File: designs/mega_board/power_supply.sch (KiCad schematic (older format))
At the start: 0 parts

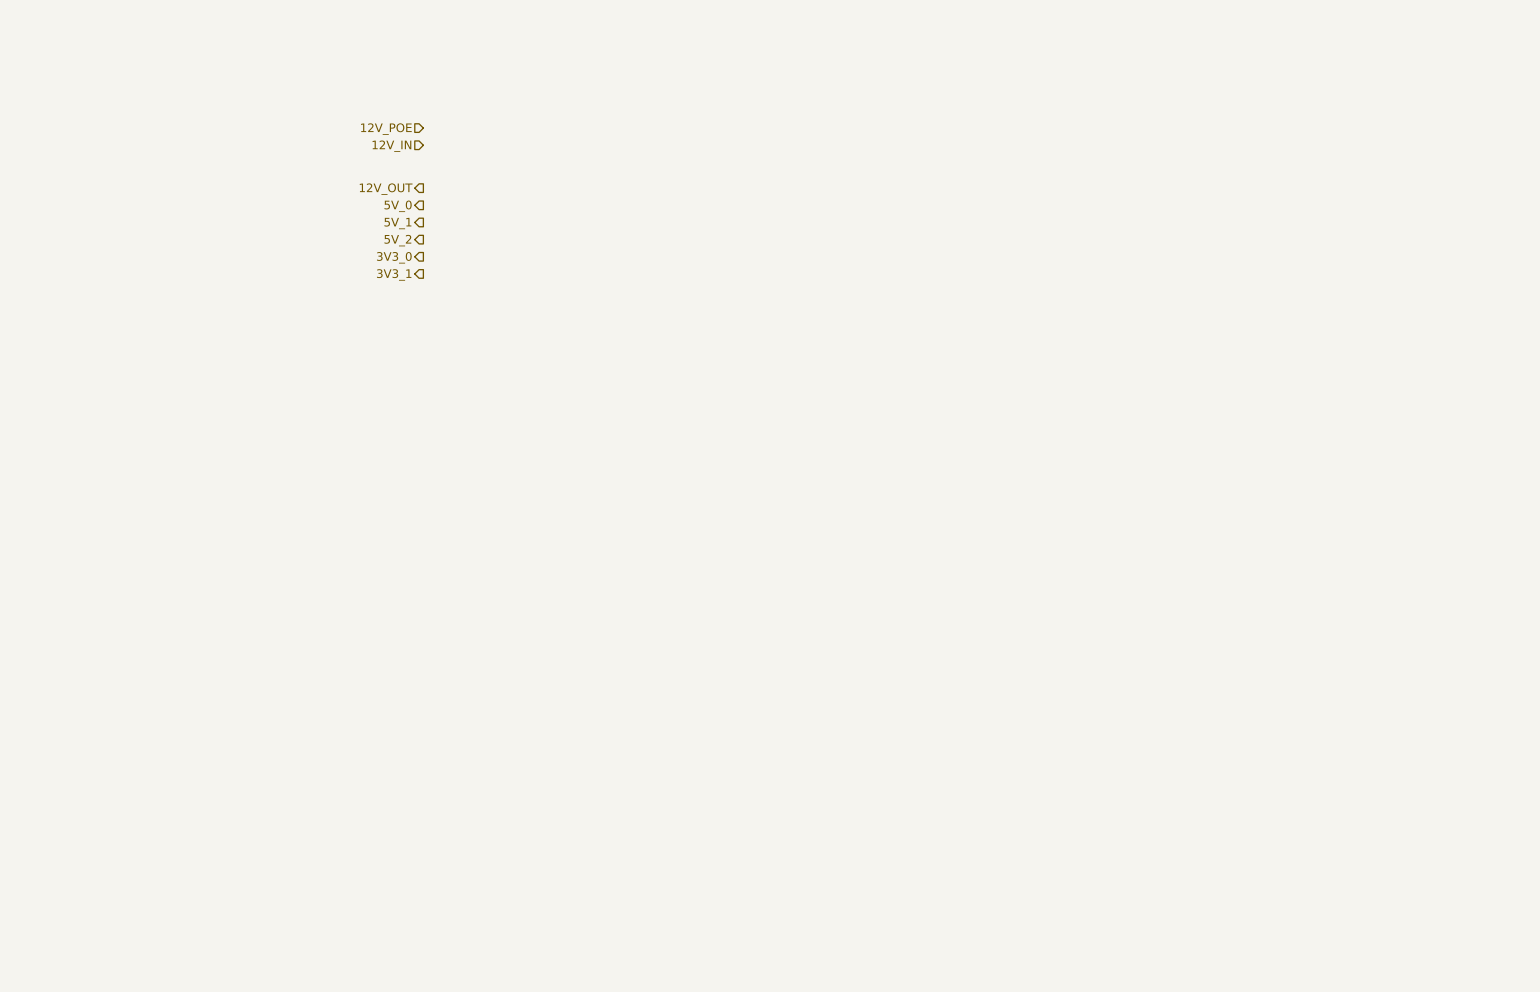
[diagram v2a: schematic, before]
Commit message: Add power supply schematic
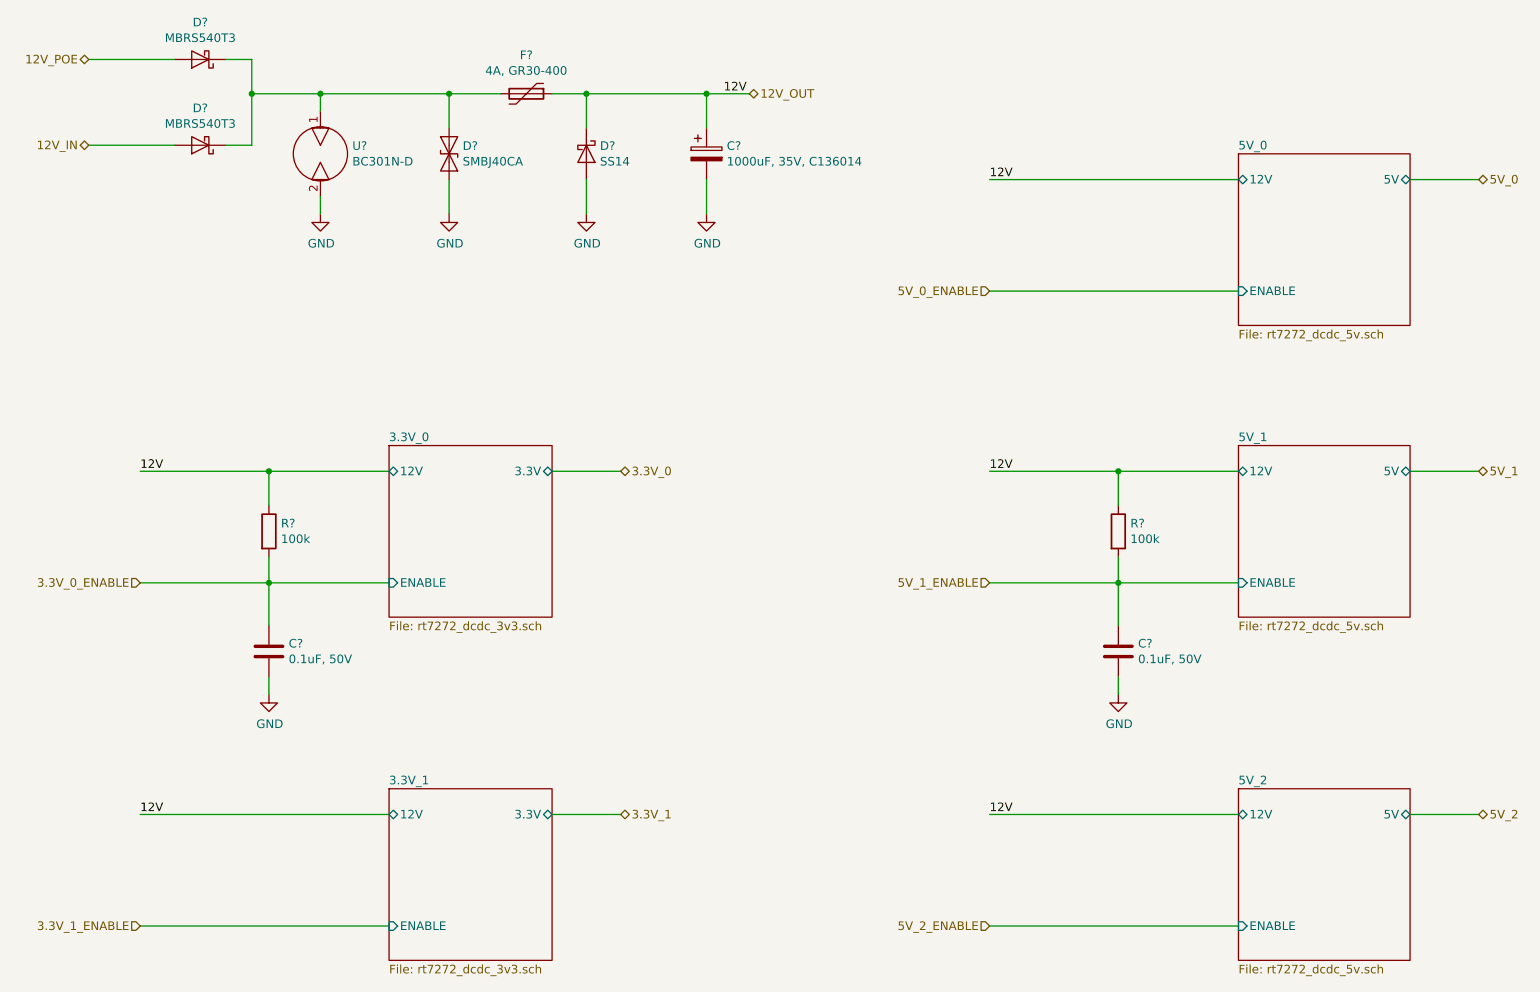
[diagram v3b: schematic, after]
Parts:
- added C? (x2): 0.1uF, 50V, symbol Device:C
- added C?: 1000uF, 35V, C136014, symbol Device:CP
- added D? (x2): MBRS540T3, symbol Device:D_Schottky
- added D?: SMBJ40CA, symbol Device:D_TVS
- added D?: SS14, symbol Device:D_Schottky
- added F?: 4A, GR30-400, symbol Device:Polyfuse
- added R? (x2): 100k, symbol Device:R
- added U?: BC301N-D, symbol BC301N-D:BC301N-D
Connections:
- net 12V_IN: now also D?.2 (A)
- net 12V_OUT: now also C?.1, D?.1 (K), F?.1, R?.1, R?.1
- net 12V_POE: now also D?.2 (A)
- new net: D?.1 (A1), D?.1 (K), D?.1 (K), F?.2, U?.1
- new net 3.3V_0_ENABLE: C?.1, R?.2
- new net 5V_1_ENABLE: C?.1, R?.2
- new net GND: C?.2, C?.2, C?.2, D?.2 (A), D?.2 (A2), U?.2

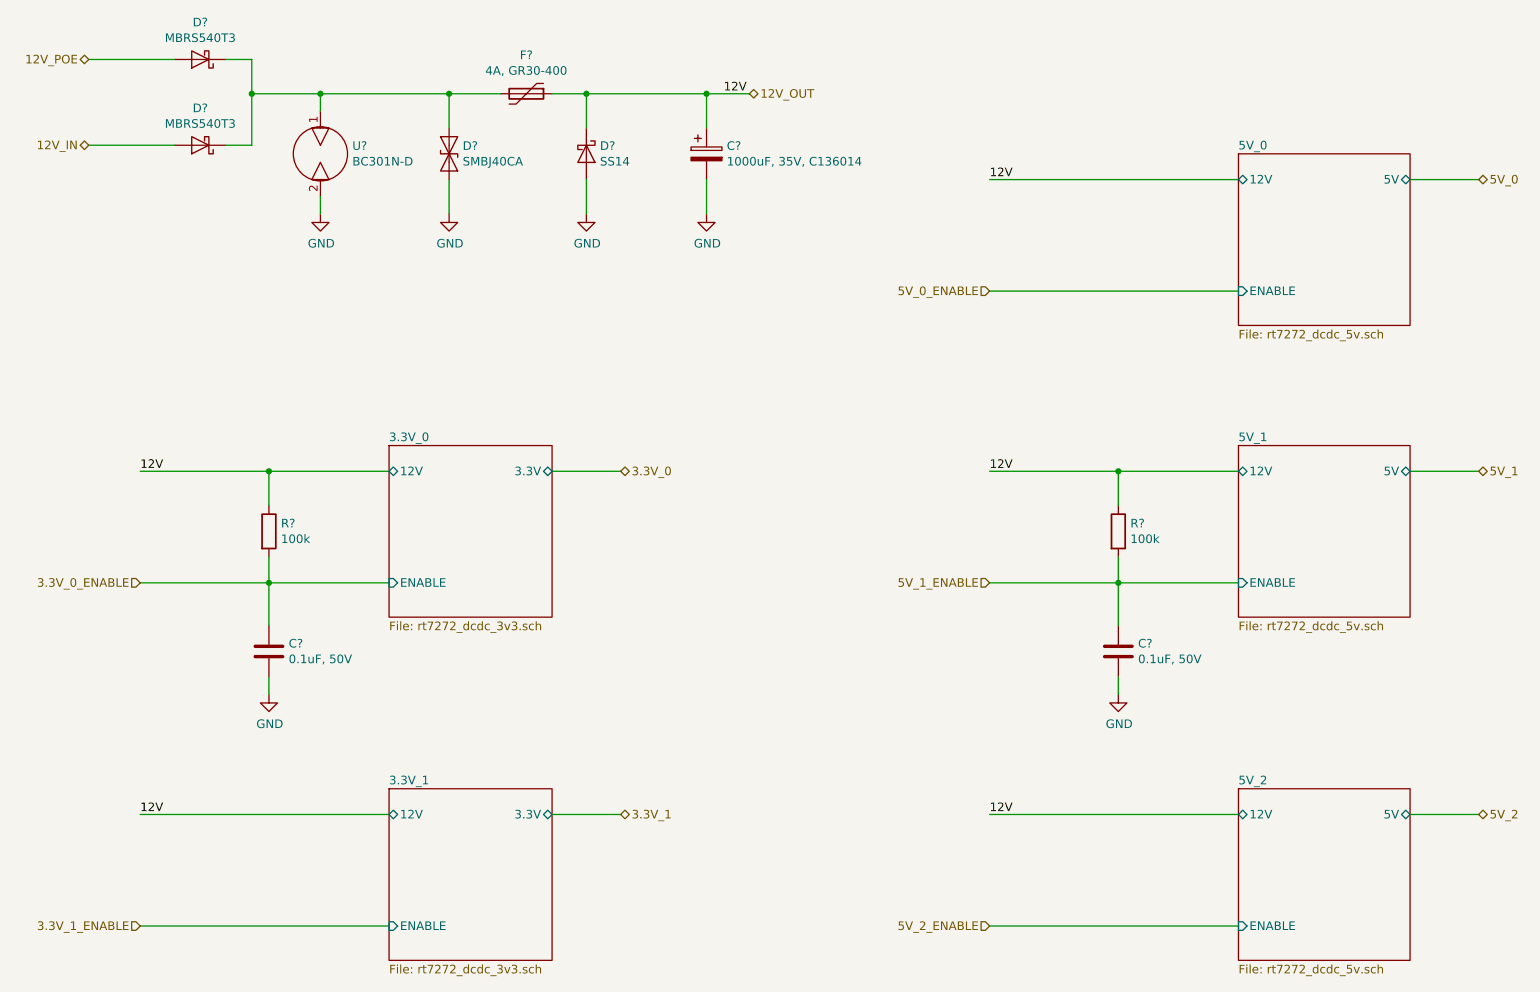
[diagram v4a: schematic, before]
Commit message: Enumerate components as is in eagle design.
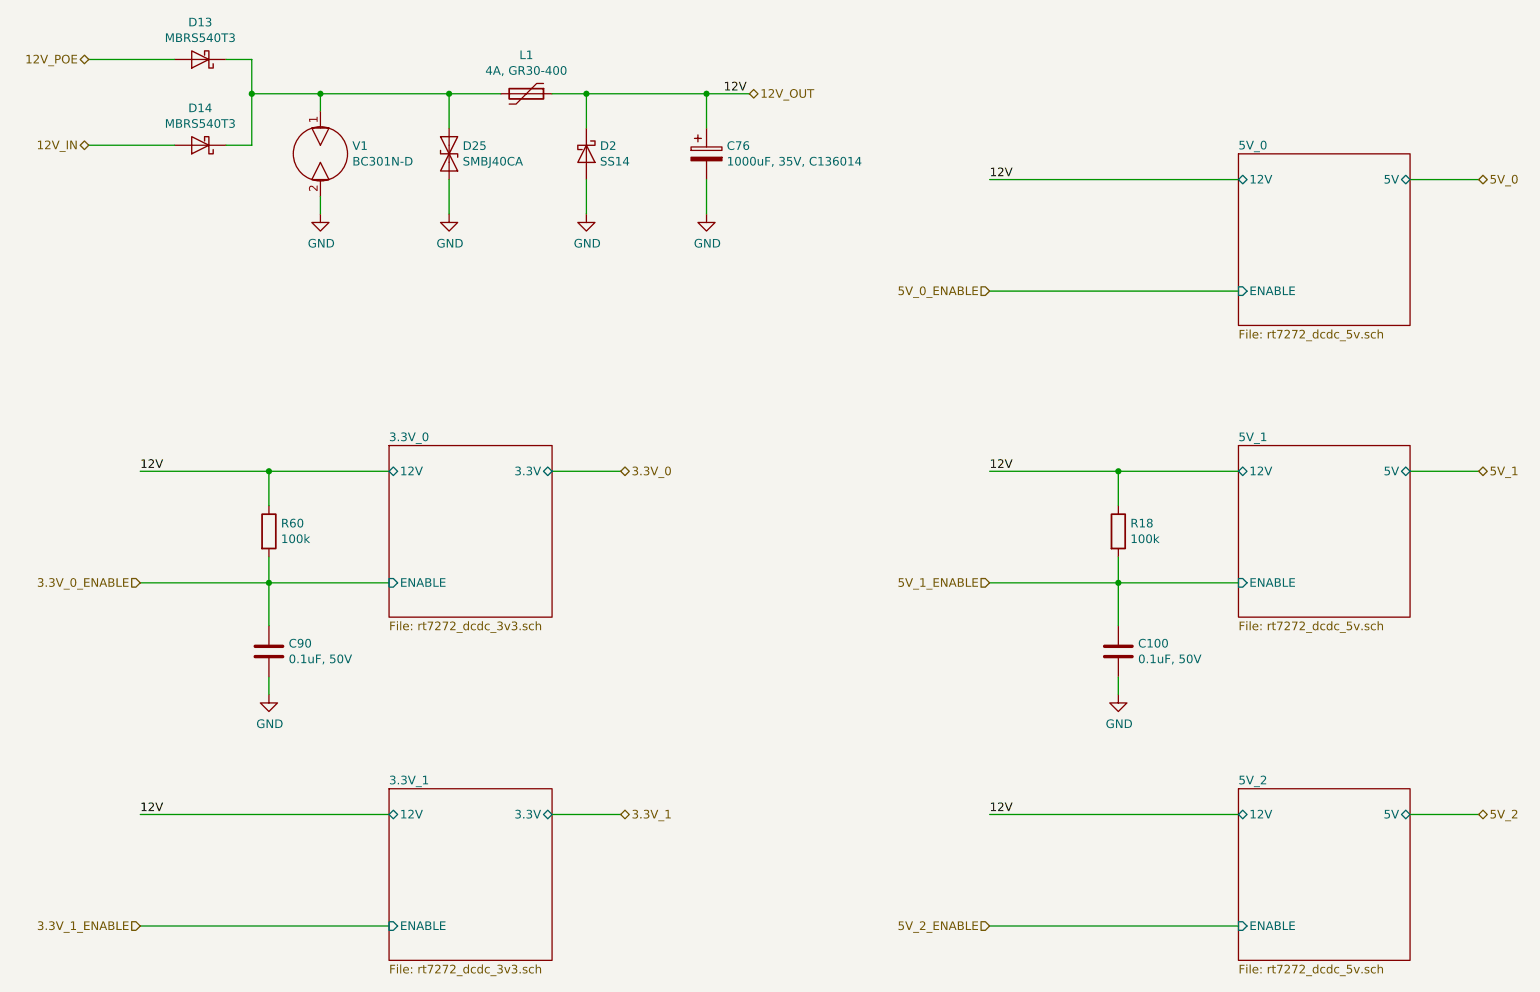
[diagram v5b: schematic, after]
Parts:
- C100, C90: renamed from C?; footprint (none) -> LibreRouter_MegaBoard:C0402
- C76: renamed from C?; footprint (none) -> LibreRouter_MegaBoard:E3,5-10
- D13, D14: renamed from D?; footprint (none) -> LibreRouter_MegaBoard:SMC
- D2: renamed from D?; footprint (none) -> LibreRouter_MegaBoard:DO214AC
- D25: renamed from D?; footprint (none) -> LibreRouter_MegaBoard:DO-214AA
- L1: renamed from F?; footprint (none) -> LibreRouter_MegaBoard:GR72-135
- R18, R60: renamed from R?; footprint (none) -> LibreRouter_MegaBoard:R0402
- V1: renamed from U?; footprint (none) -> LibreRouter_MegaBoard:BC301N-D
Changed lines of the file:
@@
 $EndSheet
 $Comp
-L Device:R R?
+L Device:R R60
 U 1 1 5D42F0F7
 P 2600 3650
-F 0 "R?" H 2670 3696 50  0000 L CNN
+F 0 "R60" H 2670 3696 50  0000 L CNN
 F 1 "100k" H 2670 3605 50  0000 L CNN
-F 2 "" V 2530 3650 50  0001 C CNN
+F 2 "LibreRouter_MegaBoard:R0402" V 2530 3650 50  0001 C CNN
 F 3 "~" H 2600 3650 50  0001 C CNN
 	1    2600 3650
@@
 $EndComp
 $Comp
-L Device:C C?
+L Device:C C90
 U 1 1 5D42F1FB
 P 2600 4350
-F 0 "C?" H 2715 4396 50  0000 L CNN
+F 0 "C90" H 2715 4396 50  0000 L CNN
 F 1 "0.1uF, 50V" H 2715 4305 50  0000 L CNN
-F 2 "" H 2638 4200 50  0001 C CNN
+F 2 "LibreRouter_MegaBoard:C0402" H 2638 4200 50  0001 C CNN
 F 3 "~" H 2600 4350 50  0001 C CNN
 	1    2600 4350
@@
 Connection ~ 2600 3950
 $Comp
-L power:GND #PWR?
+L power:GND #PWR0133
 U 1 1 5D42F2B8
 P 2600 4600
-F 0 "#PWR?" H 2600 4350 50  0001 C CNN
+F 0 "#PWR0133" H 2600 4350 50  0001 C CNN
 F 1 "GND" H 2605 4427 50  0000 C CNN
 F 2 "" H 2600 4600 50  0001 C CNN
@@
 $EndSheet
 $Comp
-L Device:R R?
+L Device:R R18
 U 1 1 5D4FE353
 P 7550 3650
-F 0 "R?" H 7620 3696 50  0000 L CNN
+F 0 "R18" H 7620 3696 50  0000 L CNN
 F 1 "100k" H 7620 3605 50  0000 L CNN
-F 2 "" V 7480 3650 50  0001 C CNN
+F 2 "LibreRouter_MegaBoard:R0402" V 7480 3650 50  0001 C CNN
 F 3 "~" H 7550 3650 50  0001 C CNN
 	1    7550 3650
@@
 $EndComp
 $Comp
-L Device:C C?
+L Device:C C100
 U 1 1 5D4FE35A
 P 7550 4350
-F 0 "C?" H 7665 4396 50  0000 L CNN
+F 0 "C100" H 7665 4396 50  0000 L CNN
 F 1 "0.1uF, 50V" H 7665 4305 50  0000 L CNN
-F 2 "" H 7588 4200 50  0001 C CNN
+F 2 "LibreRouter_MegaBoard:C0402" H 7588 4200 50  0001 C CNN
 F 3 "~" H 7550 4350 50  0001 C CNN
 	1    7550 4350
@@
 Connection ~ 7550 3950
 $Comp
-L power:GND #PWR?
+L power:GND #PWR0134
 U 1 1 5D4FE365
 P 7550 4600
-F 0 "#PWR?" H 7550 4350 50  0001 C CNN
+F 0 "#PWR0134" H 7550 4350 50  0001 C CNN
 F 1 "GND" H 7555 4427 50  0000 C CNN
 F 2 "" H 7550 4600 50  0001 C CNN
@@
 	4250 3300 4650 3300
 $Comp
-L Device:D_Schottky D?
+L Device:D_Schottky D13
 U 1 1 5D502FE5
 P 2200 900
-F 0 "D?" H 2200 684 50  0000 C CNN
+F 0 "D13" H 2200 684 50  0000 C CNN
 F 1 "MBRS540T3" H 2200 775 50  0000 C CNN
-F 2 "" H 2200 900 50  0001 C CNN
+F 2 "LibreRouter_MegaBoard:SMC" H 2200 900 50  0001 C CNN
 F 3 "~" H 2200 900 50  0001 C CNN
 	1    2200 900
@@
 $EndComp
 $Comp
-L Device:D_TVS D?
+L Device:D_TVS D25
 U 1 1 5D5030DB
 P 3650 1450
-F 0 "D?" V 3604 1529 50  0000 L CNN
+F 0 "D25" V 3604 1529 50  0000 L CNN
 F 1 "SMBJ40CA" V 3695 1529 50  0000 L CNN
-F 2 "" H 3650 1450 50  0001 C CNN
+F 2 "LibreRouter_MegaBoard:DO-214AA" H 3650 1450 50  0001 C CNN
 F 3 "~" H 3650 1450 50  0001 C CNN
 	1    3650 1450
@@
 $EndComp
 $Comp
-L Device:D_Schottky D?
+L Device:D_Schottky D2
 U 1 1 5D503196
 P 4450 1450
-F 0 "D?" V 4404 1529 50  0000 L CNN
+F 0 "D2" V 4404 1529 50  0000 L CNN
 F 1 "SS14" V 4495 1529 50  0000 L CNN
-F 2 "" H 4450 1450 50  0001 C CNN
+F 2 "LibreRouter_MegaBoard:DO214AC" H 4450 1450 50  0001 C CNN
 F 3 "~" H 4450 1450 50  0001 C CNN
 	1    4450 1450
@@
 $EndComp
 $Comp
-L Device:CP C?
+L Device:CP C76
 U 1 1 5D503338
 P 5150 1450
-F 0 "C?" H 5268 1496 50  0000 L CNN
+F 0 "C76" H 5268 1496 50  0000 L CNN
 F 1 "1000uF, 35V, C136014" H 5268 1405 50  0000 L CNN
-F 2 "" H 5188 1300 50  0001 C CNN
+F 2 "LibreRouter_MegaBoard:E3,5-10" H 5188 1300 50  0001 C CNN
 F 3 "~" H 5150 1450 50  0001 C CNN
 	1    5150 1450
@@
 $EndComp
 $Comp
-L Device:D_Schottky D?
+L Device:D_Schottky D14
 U 1 1 5D5033BC
 P 2200 1400
-F 0 "D?" H 2200 1184 50  0000 C CNN
+F 0 "D14" H 2200 1184 50  0000 C CNN
 F 1 "MBRS540T3" H 2200 1275 50  0000 C CNN
-F 2 "" H 2200 1400 50  0001 C CNN
+F 2 "LibreRouter_MegaBoard:SMC" H 2200 1400 50  0001 C CNN
 F 3 "~" H 2200 1400 50  0001 C CNN
 	1    2200 1400
@@
 $EndComp
 $Comp
-L power:GND #PWR?
+L power:GND #PWR0135
 U 1 1 5D503417
 P 3650 1800
-F 0 "#PWR?" H 3650 1550 50  0001 C CNN
+F 0 "#PWR0135" H 3650 1550 50  0001 C CNN
 F 1 "GND" H 3655 1627 50  0000 C CNN
 F 2 "" H 3650 1800 50  0001 C CNN
@@
 $EndComp
 $Comp
-L power:GND #PWR?
+L power:GND #PWR0136
 U 1 1 5D50343B
 P 4450 1800
-F 0 "#PWR?" H 4450 1550 50  0001 C CNN
+F 0 "#PWR0136" H 4450 1550 50  0001 C CNN
 F 1 "GND" H 4455 1627 50  0000 C CNN
 F 2 "" H 4450 1800 50  0001 C CNN
@@
 $EndComp
 $Comp
-L power:GND #PWR?
+L power:GND #PWR0137
 U 1 1 5D503458
 P 5150 1800
-F 0 "#PWR?" H 5150 1550 50  0001 C CNN
+F 0 "#PWR0137" H 5150 1550 50  0001 C CNN
 F 1 "GND" H 5155 1627 50  0000 C CNN
 F 2 "" H 5150 1800 50  0001 C CNN
@@
 $EndComp
 $Comp
-L Device:Polyfuse F?
+L Device:Polyfuse L1
 U 1 1 5D503666
 P 4100 1100
-F 0 "F?" V 3875 1100 50  0000 C CNN
+F 0 "L1" V 3875 1100 50  0000 C CNN
 F 1 "4A, GR30-400" V 3966 1100 50  0000 C CNN
-F 2 "" H 4150 900 50  0001 L CNN
+F 2 "LibreRouter_MegaBoard:GR72-135" H 4150 900 50  0001 L CNN
 F 3 "~" H 4100 1100 50  0001 C CNN
 	1    4100 1100
@@
 P 2900 1450
 AR Path="/5D504AD9" Ref="U?"  Part="1"
-AR Path="/5D0328DE/5D504AD9" Ref="U?"  Part="1"
-F 0 "U?" H 3086 1496 50  0000 L CNN
+AR Path="/5D0328DE/5D504AD9" Ref="V1"  Part="1"
+F 0 "V1" H 3086 1496 50  0000 L CNN
 F 1 "BC301N-D" H 3086 1405 50  0000 L CNN
-F 2 "" H 2900 1450 50  0001 C CNN
+F 2 "LibreRouter_MegaBoard:BC301N-D" H 2900 1450 50  0001 C CNN
 F 3 "" H 2900 1450 50  0001 C CNN
 	1    2900 1450
@@
 $EndComp
 $Comp
-L power:GND #PWR?
+L power:GND #PWR0138
 U 1 1 5D505643
 P 2900 1800
-F 0 "#PWR?" H 2900 1550 50  0001 C CNN
+F 0 "#PWR0138" H 2900 1550 50  0001 C CNN
 F 1 "GND" H 2905 1627 50  0000 C CNN
 F 2 "" H 2900 1800 50  0001 C CNN
